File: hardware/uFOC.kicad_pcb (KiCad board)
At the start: 2 copper layers, 54 parts, among them U1 ATSAMD21G18A-M, U2 LT3988, U3 RC4558, U4 EPC2152, U5 EPC2152, U6 INA181A2IDBVT, U7 INA181A2IDBVT, U8 EPC2152, U9 INA181A2IDBVT

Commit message: some layout
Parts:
- removed the C12 at (118.2, 25.8)
- removed the C17 at (122.4, 28.3)
- removed the C3 at (168.9, 41.8)
- removed the C4 at (168.9, 43.8)
- removed the C8 at (112.4, 20.5)
- removed the C9 at (111.9, 33.4)
- removed the R4 at (120.4, 24.5)
- added C1: 22p, Capacitor_SMD:C_0805_2012Metric, F.Cu at (139.7, 138.9)
- added C10: 1n, Capacitor_SMD:C_0805_2012Metric_Pad1.18x1.45mm_HandSolder, F.Cu at (222.2, 120.6)
- added C11: 220n, Capacitor_SMD:C_0805_2012Metric_Pad1.18x1.45mm_HandSolder, F.Cu at (210.9, 133.4)
- added C14: 22p, Capacitor_SMD:C_0402_1005Metric_Pad0.74x0.62mm_HandSolder, F.Cu at (220.1, 129.0)
- added C2: 22p, Capacitor_SMD:C_0805_2012Metric, F.Cu at (134.6, 138.9)
- added C22: ~, Capacitor_SMD:C_1210_3225Metric, F.Cu at (211.3, 117.0)
- added C23: 10u, Capacitor_SMD:C_1210_3225Metric, F.Cu at (205.6, 117.0)
- added C24: 10u, Capacitor_SMD:C_1210_3225Metric, F.Cu at (200.0, 121.3)
- added C25: 10u, Capacitor_SMD:C_1210_3225Metric, F.Cu at (200.0, 134.0)
- added C26: 10u, Capacitor_SMD:C_1210_3225Metric, F.Cu at (200.0, 117.0)
- added C27: 10u, Capacitor_SMD:C_1210_3225Metric, F.Cu at (200.0, 125.5)
- added C28: 10u, Capacitor_SMD:C_1210_3225Metric, F.Cu at (205.6, 129.8)
- added C29: 10u, Capacitor_SMD:C_1210_3225Metric, F.Cu at (211.3, 125.5)
- added C30: 10u, Capacitor_SMD:C_1210_3225Metric, F.Cu at (211.3, 129.8)
- added C31: 10u, Capacitor_SMD:C_1210_3225Metric, F.Cu at (205.6, 125.5)
- added C32: 10u, Capacitor_SMD:C_1210_3225Metric, F.Cu at (222.6, 117.0)
- added C33: 10u, Capacitor_SMD:C_1210_3225Metric, F.Cu at (216.9, 121.3)
- added C34: 10u, Capacitor_SMD:C_1210_3225Metric, F.Cu at (216.9, 125.5)
- added C35: 10u, Capacitor_SMD:C_1210_3225Metric, F.Cu at (216.9, 117.0)
- added C36: 10u, Capacitor_SMD:C_1210_3225Metric, F.Cu at (205.6, 121.3)
- added C37: 10u, Capacitor_SMD:C_1210_3225Metric, F.Cu at (211.3, 121.3)
- added C38: 10u, Capacitor_SMD:C_1210_3225Metric, F.Cu at (205.6, 134.0)
- added C39: 10u, Capacitor_SMD:C_1210_3225Metric, F.Cu at (200.0, 129.8)
- added C41: 100n, Capacitor_SMD:C_0402_1005Metric, F.Cu at (219.9, 131.0)
- added C51: 100n, Capacitor_SMD:C_0402_1005Metric, F.Cu at (211.8, 144.0)
- added C52: 10u, Capacitor_SMD:C_0805_2012Metric, F.Cu at (199.4, 148.2)
- added C53: 100n, Capacitor_SMD:C_0402_1005Metric, F.Cu at (207.4, 147.0)
- added C6: 100n, Capacitor_SMD:C_0805_2012Metric, F.Cu at (152.4, 142.0)
- added C7: 470n, Capacitor_SMD:C_0805_2012Metric_Pad1.18x1.45mm_HandSolder, F.Cu at (227.8, 116.4)
- added J1: USB_B_Micro, Connector_USB:USB_Micro-B_Molex_47346-0001, F.Cu at (154.9, 149.9)
- added J2: Conn_ARM_JTAG_SWD_10, Connector_PinHeader_1.27mm:PinHeader_2x05_P1.27mm_Vertical_SMD, F.Cu at (142.2, 129.5)
- added R1: 5k1, Resistor_SMD:R_0805_2012Metric, F.Cu at (137.2, 150.6)
- added R10: ~, Resistor_SMD:R_0805_2012Metric, F.Cu at (215.5, 135.0)
- added R12: 10k, Resistor_SMD:R_0805_2012Metric, F.Cu at (222.0, 126.6)
- added R13: 1k, Resistor_SMD:R_0805_2012Metric, F.Cu at (231.2, 119.4)
- added R14: 220, Resistor_SMD:R_0805_2012Metric, F.Cu at (226.4, 123.6)
- added R20: 220, Resistor_SMD:R_0805_2012Metric, F.Cu at (241.9, 136.7)
- added R21: 220, Resistor_SMD:R_0805_2012Metric, F.Cu at (241.9, 133.8)
- added R22: 220, Resistor_SMD:R_0805_2012Metric, F.Cu at (250.7, 133.8)
- added R24: 220, Resistor_SMD:R_0805_2012Metric, F.Cu at (246.3, 136.7)
- added R25: 220, Resistor_SMD:R_0805_2012Metric, F.Cu at (250.7, 136.7)
- added R26: 220, Resistor_SMD:R_0805_2012Metric, F.Cu at (246.3, 133.8)
- added R27: 2Meg, Resistor_SMD:R_0805_2012Metric, F.Cu at (208.1, 141.6)
- added R28: ~, Resistor_SMD:R_0805_2012Metric, F.Cu at (212.5, 141.6)
- added R29: 2Meg, Resistor_SMD:R_0805_2012Metric, F.Cu at (203.8, 148.1)
- added R30: 10k, Resistor_SMD:R_0805_2012Metric, F.Cu at (208.1, 144.5)
- added R6: 34k, Resistor_SMD:R_0805_2012Metric, F.Cu at (232.4, 116.4)
- added R8: 34k, Resistor_SMD:R_0805_2012Metric, F.Cu at (222.0, 123.6)
- added R9: ~, Resistor_SMD:R_0805_2012Metric, F.Cu at (216.3, 132.1)
- added SW1: SW_DPST, EVQ-P2402M:EVQ-P2402M, F.Cu at (149.9, 137.2)
- added U10: AS5048A, Package_SO:TSSOP-14_4.4x5mm_P0.65mm, F.Cu at (201.5, 143.4)
- added Y1: Crystal, Crystal:Crystal_SMD_MicroCrystal_CC8V-T1A-2Pin_2.0x1.2mm, F.Cu at (137.2, 139.7)
- C19: value 100n -> 22p; footprint Capacitor_SMD:C_0805_2012Metric_Pad1.18x1.45mm_HandSolder -> Capacitor_SMD:C_0402_1005Metric_Pad0.74x0.62mm_HandSolder
- C3: renamed from C1; footprint Capacitor_SMD:C_0402_1005Metric -> Capacitor_SMD:C_0805_2012Metric
- C4: renamed from C2; footprint Capacitor_SMD:C_0402_1005Metric -> Capacitor_SMD:C_0805_2012Metric
- C5: value ? -> 100n; footprint Capacitor_SMD:C_0805_2012Metric_Pad1.18x1.45mm_HandSolder -> Capacitor_SMD:C_0805_2012Metric
- R11: renamed from R6; footprint Capacitor_SMD:C_0805_2012Metric_Pad1.18x1.45mm_HandSolder -> Resistor_SMD:R_0805_2012Metric
- R2: value 10k -> 5k1; footprint Capacitor_SMD:C_0805_2012Metric_Pad1.18x1.45mm_HandSolder -> Resistor_SMD:R_0805_2012Metric
- R3: value 34k -> 5k1; footprint Capacitor_SMD:C_0805_2012Metric_Pad1.18x1.45mm_HandSolder -> Resistor_SMD:R_0805_2012Metric
- R5: value 34k -> 10k; footprint Capacitor_SMD:C_0805_2012Metric_Pad1.18x1.45mm_HandSolder -> Resistor_SMD:R_0805_2012Metric
- R7: footprint Capacitor_SMD:C_0805_2012Metric_Pad1.18x1.45mm_HandSolder -> Resistor_SMD:R_0805_2012Metric
- moved R5 140.9 mm to (226.8, 120.6), turned to 0 degrees
- moved C19 137.4 mm to (210.1, 135.9)
- moved R7 137.2 mm to (216.3, 129.1)
- moved C5 130.2 mm to (144.0, 152.4), turned to 90 degrees
- moved R3 130.1 mm to (137.2, 148.6), turned to 180 degrees
- moved R2 123.5 mm to (137.2, 146.6), turned to 180 degrees
- moved C4 108.9 mm to (137.2, 144.5), turned to 0 degrees
- moved U1 102.8 mm to (144.8, 144.8)
- moved C3 101.0 mm to (144.5, 137.2), turned to -90 degrees
- moved C12 78.2 mm to (144.3, 108.8)
- moved C15 78.2 mm to (150.3, 108.8)
- moved C17 78.2 mm to (143.1, 115.5)
- moved C43 78.2 mm to (144.8, 73.8)
- moved C45 78.2 mm to (140.0, 73.8)
- moved C46 78.2 mm to (140.0, 82.8)
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- renumbered C10 to C12, C11 to C13, C13 to C15, C14 to C16, C15 to C17, C16 to C18, C18 to C20, C20 to C42, C21 to C43, C22 to C44, C23 to C45, C24 to C46, C25 to C47, C26 to C48, C27 to C49, C28 to C50, C6 to C8, C7 to C9, R8 to R15, R9 to R16, R10 to R17, R11 to R18, R12 to R19, R13 to R23, R1 to R4
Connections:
- net PH_A renamed PH_U
- net PH_B renamed PH_V
- net PH_C renamed PH_W
- net VCC renamed VS
- C12 pad 2: GND -> GNDPWR
- C13 pad 2: GND -> GNDPWR
- C15 pad 2: GND -> GNDPWR
- C17 pad 2: GND -> GNDPWR
- C18 pad 1: GND -> GNDPWR
- C19 pad 2: GND -> Net-(C19-Pad2)
- C20 pad 1: GND -> GNDPWR
- C3 pad 1: GNDD -> GND
- C4 pad 1: GNDD -> GND
- C42 pad 1: VDD -> +12V
- C43 pad 1: VDD -> +12V
- C48 pad 1: VDD -> +12V
- C5 pad 2: VDD -> +3V3
- C8 pad 2: GND -> GNDPWR
- C9 pad 2: GND -> GNDPWR
- L1 pad 1: VDD -> +12V
- R11 pad 2: Net-(R6-Pad2) -> Net-(R11-Pad2)
- R2 pad 1: GND -> /Microcontroller/A1
- R2 pad 2: Net-(R1-Pad1) -> ISNS_A
- R3 pad 1: Net-(R3-Pad1) -> /Microcontroller/A2
- R3 pad 2: GND -> ISNS_B
- R4 pad 1: Net-(R1-Pad1) -> Net-(R4-Pad1)
- R4 pad 2: VDD -> +12V
- R5 pad 1: +3V3 -> Net-(R4-Pad1)
- R5 pad 2: Net-(C17-Pad1) -> GNDPWR
- R7 pad 1: Net-(R6-Pad2) -> Net-(C19-Pad2)
- R7 pad 2: GND -> GNDPWR
- U1 pad 1: unconnected-(U1-Pad1) -> Net-(U1-Pad1)
- U1 pad 10: unconnected-(U1-Pad10) -> WH
- U1 pad 11: unconnected-(U1-Pad11) -> /Microcontroller/D8
- U1 pad 12: ISNS_C -> /Microcontroller/D9
- U1 pad 13: unconnected-(U1-Pad13) -> /Microcontroller/D4
- U1 pad 14: unconnected-(U1-Pad14) -> /Microcontroller/D3
- U1 pad 15: unconnected-(U1-Pad15) -> /Microcontroller/D1
- U1 pad 16: unconnected-(U1-Pad16) -> /Microcontroller/D0
- U1 pad 18: GNDD -> GND
- U1 pad 19: unconnected-(U1-Pad19) -> MOSI
- U1 pad 2: unconnected-(U1-Pad2) -> Net-(C2-Pad1)
- U1 pad 20: unconnected-(U1-Pad20) -> SCK
- U1 pad 21: unconnected-(U1-Pad21) -> MISO
- U1 pad 23: unconnected-(U1-Pad23) -> /Microcontroller/D2
- U1 pad 24: unconnected-(U1-Pad24) -> UL
- U1 pad 25: unconnected-(U1-Pad25) -> VH
- U1 pad 26: unconnected-(U1-Pad26) -> /Microcontroller/D13
- U1 pad 27: unconnected-(U1-Pad27) -> VL
- U1 pad 28: unconnected-(U1-Pad28) -> WL
- U1 pad 29: unconnected-(U1-Pad29) -> UH
- U1 pad 3: unconnected-(U1-Pad3) -> /Microcontroller/A0
- U1 pad 30: unconnected-(U1-Pad30) -> /Microcontroller/D7
- U1 pad 31: unconnected-(U1-Pad31) -> /Microcontroller/SDA
- U1 pad 32: unconnected-(U1-Pad32) -> /Microcontroller/SCL
- U1 pad 35: GNDD -> GND
- U1 pad 37: unconnected-(U1-Pad37) -> /Microcontroller/TXD
- U1 pad 38: unconnected-(U1-Pad38) -> /Microcontroller/RXD
- U1 pad 39: unconnected-(U1-Pad39) -> /Microcontroller/TXLED
- U1 pad 4: ISNS_A -> /Microcontroller/AREF
- U1 pad 40: unconnected-(U1-Pad40) -> Net-(SW1-Pad1)
- U1 pad 41: unconnected-(U1-Pad41) -> /Microcontroller/USBHOSTEN
- U1 pad 42: GNDD -> GND
- U1 pad 45: unconnected-(U1-Pad45) -> /Microcontroller/SWCLK
- U1 pad 46: unconnected-(U1-Pad46) -> /Microcontroller/SWDIO
- U1 pad 47: unconnected-(U1-Pad47) -> /Microcontroller/A5
- U1 pad 48: unconnected-(U1-Pad48) -> /Microcontroller/RXLED
- U1 pad 49: GNDD -> GND
- U1 pad 5: GNDD -> GND
- U1 pad 7: unconnected-(U1-Pad7) -> /Microcontroller/A1
- U1 pad 8: unconnected-(U1-Pad8) -> /Microcontroller/A2
- U1 pad 9: ISNS_B -> /Microcontroller/A3
- U2 pad 11: Net-(C17-Pad1) -> Net-(C19-Pad2)
- U2 pad 12: GND -> GNDPWR
- U2 pad 13: Net-(R3-Pad1) -> Net-(R6-Pad2)
- U2 pad 14: Net-(R1-Pad1) -> Net-(R4-Pad1)
- U2 pad 17: GND -> GNDPWR
- U3 pad 3: Net-(R6-Pad2) -> Net-(R11-Pad2)
- U4 pad 2: VDD -> +12V
- U4 pad 3: PWM_AT -> UH
- U4 pad 4: PWM_AB -> UL
- U5 pad 2: VDD -> +12V
- U5 pad 3: PWM_CT -> WH
- U5 pad 4: PWM_CB -> WL
- U8 pad 2: VDD -> +12V
- U8 pad 3: PWM_BT -> VH
- U8 pad 4: PWM_BB -> VL
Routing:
- net GND: track 2.25 -> 15.2 mm
- net /Microcontroller/SWCLK: track 0.00 -> 12.9 mm
- net Net-(R4-Pad1): track 0.00 -> 12.4 mm, vias 0 -> 2
- net Net-(R1-Pad1): track 12.4 -> 0.00 mm, vias 2 -> 0
- net /Microcontroller/SWDIO: track 0.00 -> 11.2 mm
- net /Microcontroller/D+: track 0.00 -> 11.0 mm
- net /Microcontroller/D-: track 0.00 -> 11.0 mm
- net Net-(C2-Pad1): track 0.00 -> 10.5 mm
- net +3V3: track 15.0 -> 24.7 mm
- net Net-(C17-Pad1): track 9.52 -> 0.00 mm, vias 2 -> 0
- net Net-(C19-Pad2): track 0.00 -> 9.52 mm, vias 0 -> 2
- net /Microcontroller/A3: track 0.00 -> 6.81 mm
- net /Microcontroller/A2: track 0.00 -> 5.43 mm
- net Net-(U1-Pad1): track 0.00 -> 5.18 mm
- net +12V: track 0.00 -> 4.00 mm
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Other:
- copper layers 2 -> 4

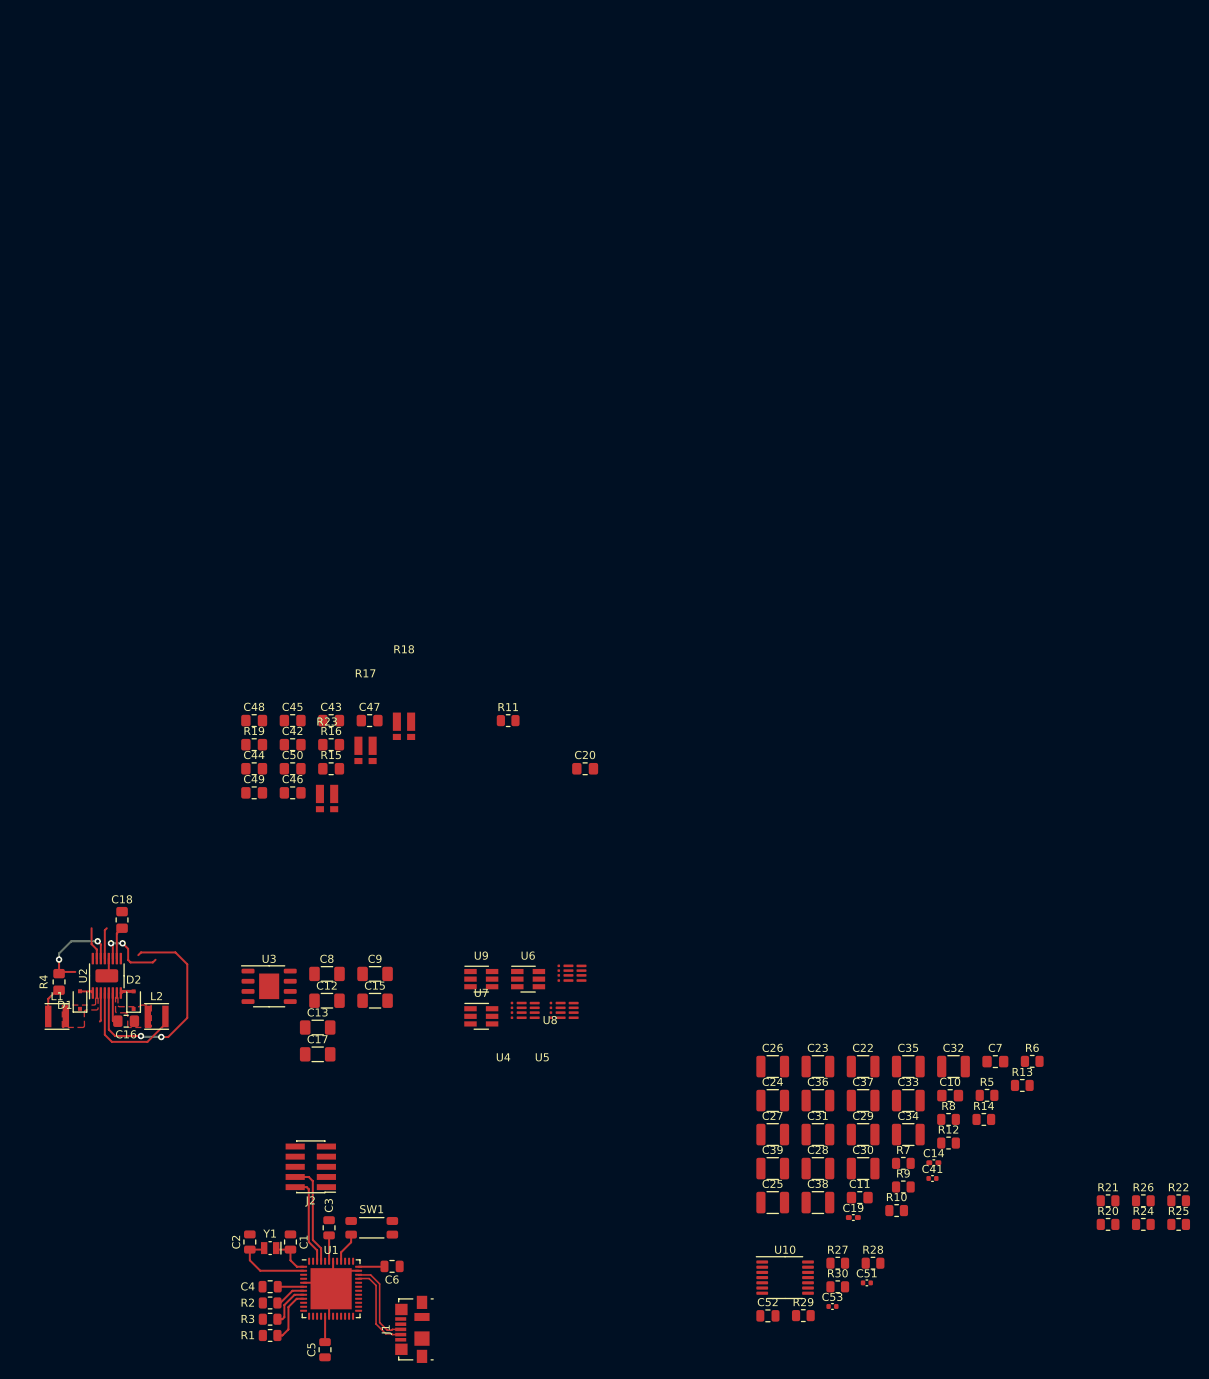
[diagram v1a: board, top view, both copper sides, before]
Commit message: Simplified sensing, added some power layout.
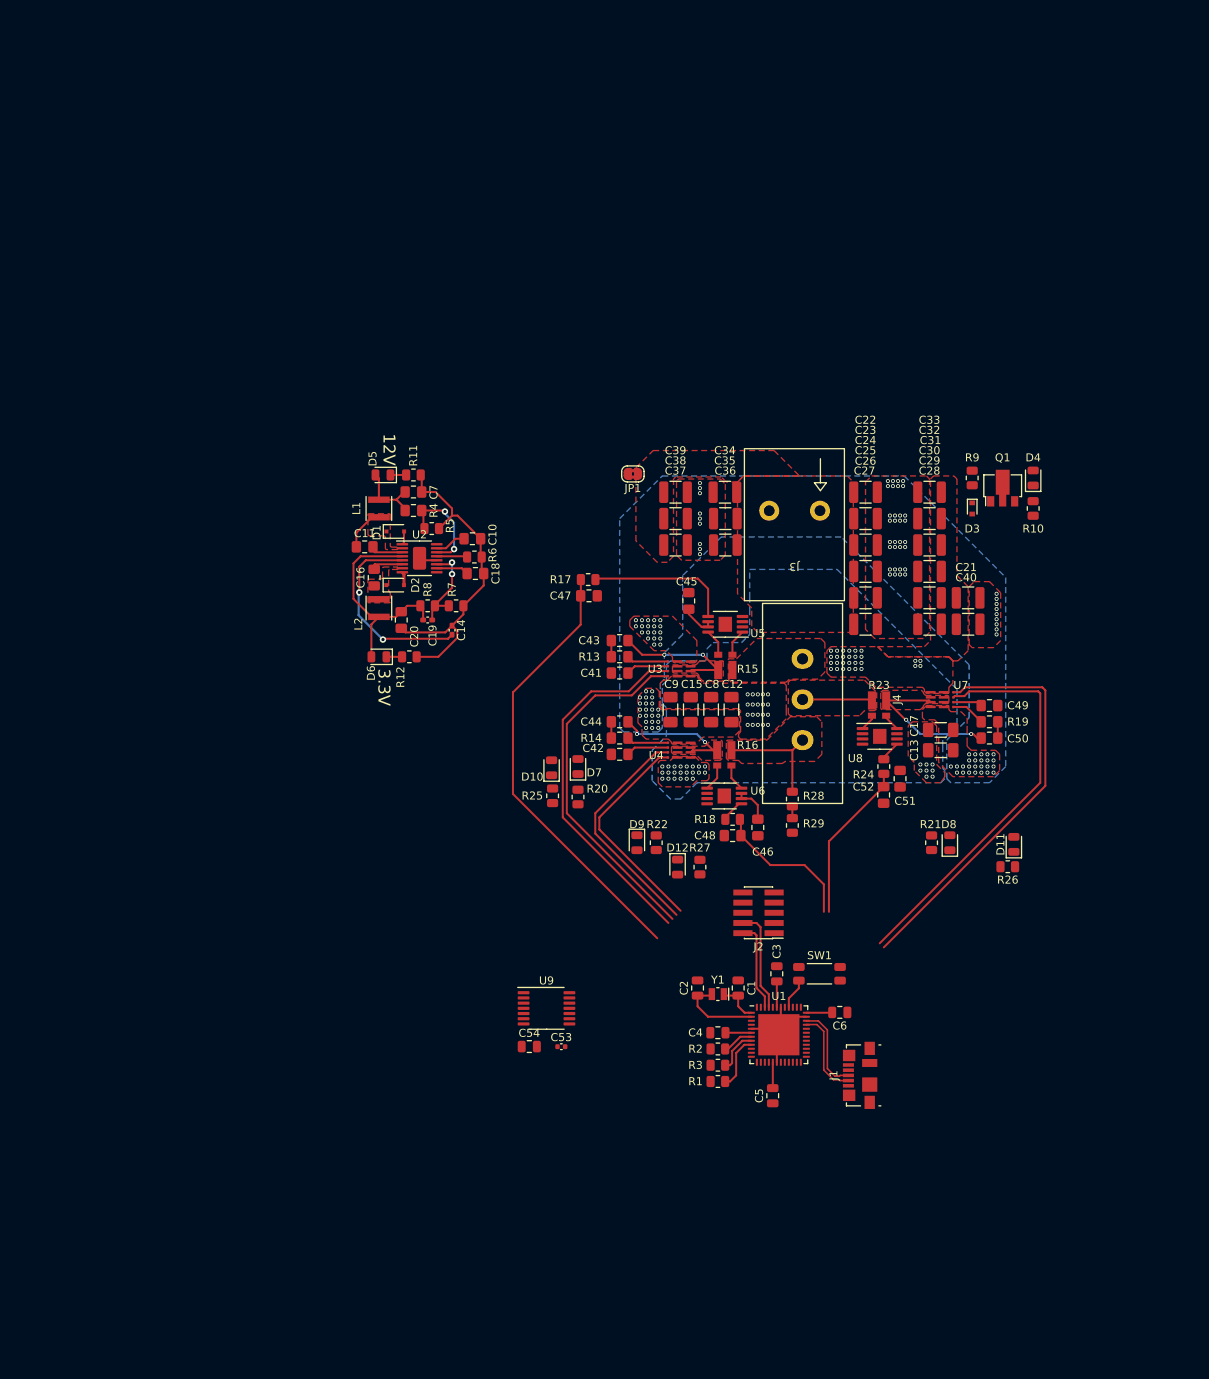
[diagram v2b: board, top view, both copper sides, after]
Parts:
- removed the C41 at (219.9, 131.0)
- removed the C50 at (140.0, 79.8)
- removed the C53 at (207.4, 147.0)
- removed the R11 at (166.9, 73.8)
- removed the R12 at (222.0, 126.6)
- removed the R27 at (208.1, 141.6)
- removed R30: 10k, Resistor_SMD:R_0805_2012Metric
- removed the U3 at (137.0, 107.0)
- removed the U7 at (163.6, 110.7)
- removed the U9 at (163.6, 106.1)
- added C21: ~, Capacitor_SMD:C_1210_3225Metric, F.Cu at (224.4, 58.4)
- added C40: ~, Capacitor_SMD:C_1210_3225Metric, F.Cu at (224.4, 61.7)
- added C45: 100n, Capacitor_SMD:C_0805_2012Metric_Pad1.18x1.45mm_HandSolder, F.Cu at (189.5, 58.8)
- added C48: 4.7n, Capacitor_SMD:C_0805_2012Metric_Pad1.18x1.45mm_HandSolder, F.Cu at (195.0, 88.1)
- added C51: 100n, Capacitor_SMD:C_0805_2012Metric_Pad1.18x1.45mm_HandSolder, F.Cu at (215.9, 81.0)
- added C52: 4.7n, Capacitor_SMD:C_0805_2012Metric_Pad1.18x1.45mm_HandSolder, F.Cu at (213.8, 83.1)
- added D10: LED, LED_SMD:LED_0805_2012Metric, F.Cu at (172.3, 79.7)
- added D11: LED, LED_SMD:LED_0805_2012Metric, F.Cu at (230.1, 89.2)
- added D12: LED, LED_SMD:LED_0805_2012Metric, F.Cu at (188.1, 92.1)
- added D3: ~, Diode_SMD:D_SOD-523, F.Cu at (224.9, 47.2)
- added D4: LED, LED_SMD:LED_0805_2012Metric, F.Cu at (232.5, 43.4)
- added D5: LED, LED_SMD:LED_0805_2012Metric, F.Cu at (151.3, 43.1)
- added D6: LED, LED_SMD:LED_0805_2012Metric, F.Cu at (150.8, 65.8)
- added D7: LED, LED_SMD:LED_0805_2012Metric, F.Cu at (175.6, 79.5)
- added D8: LED, LED_SMD:LED_0805_2012Metric, F.Cu at (222.1, 89.0)
- added D9: LED, LED_SMD:LED_0805_2012Metric, F.Cu at (183.0, 89.0)
- added J3: Conn_01x02_Female, SnapEDA Library:1720033, F.Cu at (202.7, 47.5)
- added J4: Conn_01x03_Female, SnapEDA Library:1716090000, F.Cu at (203.7, 71.1)
- added JP1: Jumper_2_Bridged, Jumper:SolderJumper-2_P1.3mm_Bridged2Bar_RoundedPad1.0x1.5mm, F.Cu at (182.5, 42.9)
- added Q1: ~, Package_TO_SOT_SMD:SOT-89-3, F.Cu at (228.7, 44.7)
- added R17: 100, Resistor_SMD:R_0805_2012Metric, F.Cu at (176.9, 56.1)
- added R18: 100, Resistor_SMD:R_0805_2012Metric, F.Cu at (195.0, 86.1)
- added R24: 100, Resistor_SMD:R_0805_2012Metric, F.Cu at (213.9, 79.5)
- added U5: AD8418, Package_SO:MSOP-8-1EP_3x3mm_P0.65mm_EP1.68x1.88mm, F.Cu at (194.1, 61.7)
- added U8: AD8418, Package_SO:MSOP-8-1EP_3x3mm_P0.65mm_EP1.68x1.88mm, F.Cu at (213.4, 75.7)
- C47: value 100n -> 4.7n
- R28: value ~ -> 39k
- R29: value 2Meg -> 2.2k
- U6: value INA181A2IDBVT -> AD8418; footprint Package_TO_SOT_SMD:SOT-23-6_Handsoldering -> Package_SO:MSOP-8-1EP_3x3mm_P0.65mm_EP1.68x1.88mm
- moved R11 107.8 mm to (155.1, 43.1)
- moved C11 102.2 mm to (149.0, 52.0)
- moved C7 101.8 mm to (155.1, 45.2), turned to 180 degrees
- moved R5 99.2 mm to (157.4, 49.8)
- moved R6 94.0 mm to (162.7, 53.3), turned to 180 degrees
- moved R12 92.2 mm to (154.6, 65.8)
- moved C50 92.2 mm to (227.1, 75.9)
- moved R19 92.0 mm to (227.1, 73.9), turned to 180 degrees
- moved C49 91.9 mm to (227.1, 71.9)
- moved C10 91.7 mm to (162.4, 51.0), turned to 180 degrees
- moved C19 91.7 mm to (156.8, 61.2)
- moved R8 91.4 mm to (156.8, 59.4)
- moved R25 91.2 mm to (172.5, 83.2), turned to -90 degrees
- moved C14 89.8 mm to (159.9, 62.5), turned to -90 degrees
- moved R10 89.4 mm to (232.5, 47.2), turned to -90 degrees
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- renumbered C42 to C41, C43 to C42, C44 to C43, C45 to C44, C48 to C49, C49 to C50, C51 to C53, C52 to C54, R13 to R11, R14 to R12, R15 to R13, R16 to R14, R17 to R15, R18 to R16, R24 to R25, R25 to R26, R26 to R27, U4 to U3, U5 to U4, U8 to U7, U10 to U9
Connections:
- C43 pad 1: Net-(C44-Pad1) -> Net-(C43-Pad1)
- C44 pad 1: Net-(C45-Pad1) -> Net-(C44-Pad1)
- C47 pad 1: +3V3 -> GND
- C47 pad 2: GND -> ISNS_A
- C50 pad 1: Net-(C49-Pad1) -> Net-(C50-Pad1)
- R10 pad 2: GND -> GNDPWR
- R11 pad 2: GND -> GNDPWR
- R12 pad 2: GND -> GNDPWR
- R15 pad 1: Net-(C44-Pad1) -> PH_U
- R15 pad 2: PH_U -> Net-(C43-Pad1)
- R16 pad 1: Net-(C45-Pad1) -> Net-(C44-Pad1)
- R23 pad 1: Net-(C49-Pad1) -> PH_V
- R23 pad 2: PH_V -> Net-(C50-Pad1)
- R28 pad 1: Net-(R27-Pad2) -> VSNS_W
- R28 pad 2: VAA -> PH_W
- R29 pad 2: Net-(R29-Pad2) -> VSNS_W
- R9 pad 1: +3V3 -> VS
- U3 pad 6: Net-(C44-Pad1) -> Net-(C43-Pad1)
- U3 pad 7: GND -> GNDPWR
- U4 pad 6: Net-(C45-Pad1) -> Net-(C44-Pad1)
- U4 pad 7: GND -> GNDPWR
- U6 pad 1: ISNS_A -> Net-(C44-Pad1)
- U6 pad 3: Net-(C44-Pad1) -> GND
- U6 pad 4: PH_U -> unconnected-(U6-Pad4)
- U6 pad 5: unconnected-(U6-Pad5) -> Net-(R18-Pad1)
- U7 pad 6: Net-(C49-Pad1) -> Net-(C50-Pad1)
- U7 pad 7: GND -> GNDPWR
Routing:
- net ISNS_A: track 0.00 -> 55.8 mm
- net VL: track 0.00 -> 52.4 mm
- net VH: track 0.00 -> 50.8 mm
- net UH: track 0.00 -> 46.5 mm
- net UL: track 0.00 -> 45.0 mm
- net GNDPWR: track 2.25 -> 44.5 mm, vias 0 -> 78
- net WH: track 0.00 -> 29.1 mm
- net WL: track 0.00 -> 27.6 mm
- net +3V3: track 24.7 -> 46.9 mm
- net Net-(C50-Pad1): track 0.00 -> 21.6 mm, vias 0 -> 2
- net ISNS_B: track 0.00 -> 20.1 mm
- net Net-(C43-Pad1): track 0.00 -> 19.7 mm, vias 0 -> 2
- net Net-(C44-Pad1): track 0.00 -> 19.7 mm, vias 0 -> 2
- net +12V: track 4.00 -> 23.1 mm
- net ISNS_C: track 0.00 -> 18.4 mm
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- added copper zone on B.Cu, net GNDPWR
- added copper zone on F.Cu, net GNDPWR
- added copper zone on F.Cu, net Net-(C43-Pad1)
- added copper zone on F.Cu, net Net-(C44-Pad1)
- added copper zone on F.Cu, net Net-(C50-Pad1)
- added copper zone on F.Cu, net PH_U
- added copper zone on F.Cu, net PH_V
- added copper zone on F.Cu, net PH_W
- added copper zone on B.Cu, net VS
- added copper zone on F.Cu, net VS
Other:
- board text added: "12V"
- board text added: "3.3V"
